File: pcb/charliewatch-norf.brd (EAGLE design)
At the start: 30.5 x 30.5 mm, 84 parts, among them U2 CC430F5137IRGZR, X1 CRYSTALS-NOGND-IQXC-25

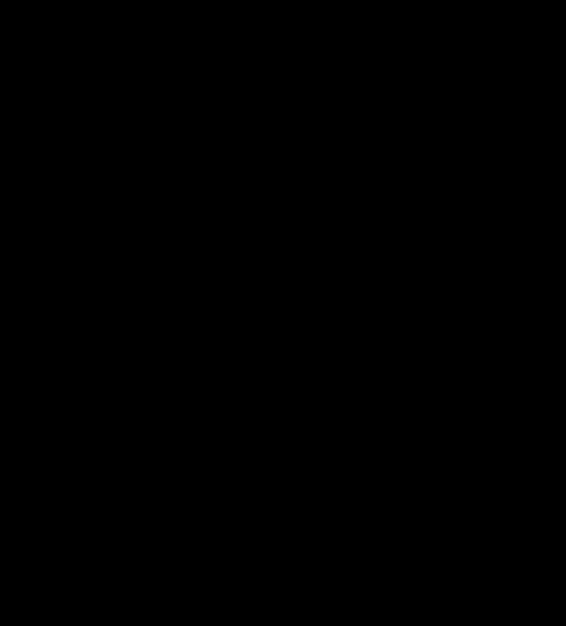
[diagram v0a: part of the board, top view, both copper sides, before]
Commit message: Add LIS3DH Accelerometer
LIS3DH is an i2c accelerometer. Hope to use this to control the watch
with tap based gestures
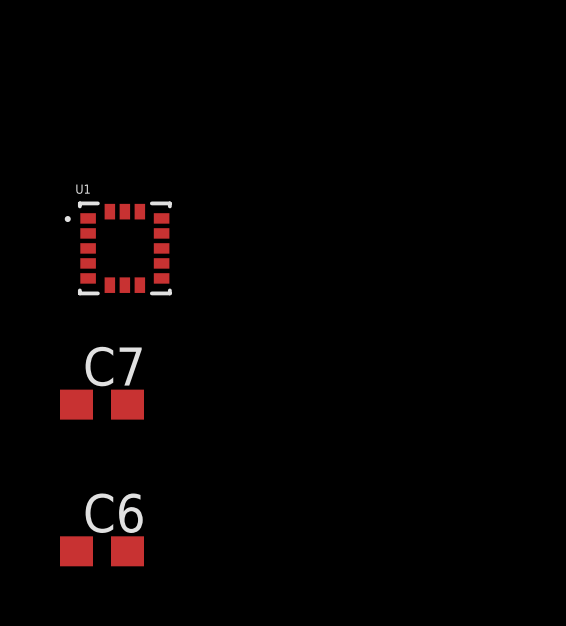
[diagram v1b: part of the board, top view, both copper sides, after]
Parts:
- added C6: 10uF, resistor:C0603
- added C7: 0.1uF, resistor:C0603
- added U1: LIS3DH, LIS3DH:PQFN50P300X300X100-16N
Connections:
- new net IMU_INT: U1.11, U2.13
- new net IMU_SCL: U1.4, U2.11
- new net IMU_SDA: U1.6, U2.10
- net GND: now also C6.2, C7.2, U1.10, U1.12, U1.5, U1.7
- net VCC: now also C6.1, C7.1, U1.1, U1.14, U1.8
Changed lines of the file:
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@@
 <?xml version="1.0" encoding="utf-8"?>
 <!DOCTYPE eagle SYSTEM "eagle.dtd">
-<eagle version="7.7.0">
+<eagle version="9.4.0">
 <drawing>
 <settings>
 <setting alwaysvectorfont="no"/>
+<setting keepoldvectorfont="yes"/>
 <setting verticaltext="up"/>
 </settings>
@@
 <param name="dpMaxLengthDifference" value="10mm"/>
 <param name="dpGapFactor" value="2.5"/>
-<param name="checkGrid" value="0"/>
 <param name="checkAngle" value="0"/>
 <param name="checkFont" value="1"/>
 <param name="checkRestrict" value="1"/>
+<param name="checkStop" value="0"/>
+<param name="checkValues" value="0"/>
+<param name="checkNames" value="1"/>
+<param name="checkWireStubs" value="1"/>
+<param name="checkPolygonWidth" value="0"/>
 <param name="useDiameter" value="13"/>
 <param name="maxErrors" value="50"/>
@@
 <element name="X1" library="IQD-Frequency-Products" package="2.0X1.2-2PAD" value="CRYSTALS-NOGND-IQXC-25" x="24.4475" y="31.115" smashed="yes" rot="R180"/>
 <element name="U2" library="Texas Instruments_By_element14_Batch_1" package="QFN50P700X700X100-49N" value="CC430F5137IRGZR" x="25.4" y="25.4" smashed="yes">
+<attribute name="MPN" value="CC430F5137IRGZR" x="25.4" y="25.4" size="1.778" layer="27" display="off"/>
+<attribute name="OC_FARNELL" value="-" x="25.4" y="25.4" size="1.778" layer="27" display="off"/>
+<attribute name="OC_NEWARK" value="68R5912" x="25.4" y="25.4" size="1.778" layer="27" display="off"/>
 <attribute name="PACKAGE" value="QFN-48" x="25.4" y="25.4" size="1.778" layer="27" display="off"/>
 <attribute name="SUPPLIER" value="TEXAS INSTRUMENTS" x="25.4" y="25.4" size="1.778" layer="27" display="off"/>
-<attribute name="OC_FARNELL" value="-" x="25.4" y="25.4" size="1.778" layer="27" display="off"/>
-<attribute name="MPN" value="CC430F5137IRGZR" x="25.4" y="25.4" size="1.778" layer="27" display="off"/>
-<attribute name="OC_NEWARK" value="68R5912" x="25.4" y="25.4" size="1.778" layer="27" display="off"/>
 </element>
 <element name="R1" library="rcl" package="R0402" value="75k" x="27.94" y="31.0515" smashed="yes">
@@
 </element>
 <element name="S2" library="SparkFun-Switches" package="TACTILE_SWITCH_SMD_RIGHT_ANGLE" value="MOMENTARY-SWITCH-SPST-SMD-RIGHT-ANGLE" x="38.1635" y="25.4" smashed="yes" rot="MR270">
+<attribute name="NAME" x="36.5125" y="25.4" size="0.6096" layer="26" font="vector" ratio="20" rot="MR270" align="bottom-center"/>
 <attribute name="PROD_ID" value="COMP-12265" x="38.1635" y="25.4" size="1.778" layer="28" rot="MR270" display="off"/>
-<attribute name="NAME" x="36.5125" y="25.4" size="0.6096" layer="26" font="vector" ratio="20" rot="MR270" align="bottom-center"/>
+</element>
+<element name="U1" library="LIS3DH" package="PQFN50P300X300X100-16N" value="LIS3DH" x="0.127" y="3.3655" smashed="yes">
+<attribute name="AVAILABILITY" value="Unavailable" x="-4.0005" y="8.509" size="1.778" layer="27" display="off"/>
+<attribute name="DESCRIPTION" value=" MEMS digital output motion sensor ultra low-power high performance 3-axes nano accelerometer " x="-4.0005" y="8.509" size="1.778" layer="27" display="off"/>
+<attribute name="MF" value="STMicroelectronics" x="-4.0005" y="8.509" size="1.778" layer="27" display="off"/>
+<attribute name="MP" value="LIS3DH" x="-4.0005" y="8.509" size="1.778" layer="27" display="off"/>
+<attribute name="NAME" x="-1.5242" y="5.18971875" size="0.3048375" layer="25"/>
+<attribute name="PACKAGE" value="LGA-16 STMicroelectronics" x="-4.0005" y="8.509" size="1.778" layer="27" display="off"/>
+<attribute name="PRICE" value="None" x="-4.0005" y="8.509" size="1.778" layer="27" display="off"/>
+<attribute name="VALUE" x="-1.6039" y="1.18336875" size="0.304959375" layer="27"/>
+</element>
+<element name="C6" library="resistor" package="C0603" value="10uF" x="-0.635" y="-6.731" smashed="yes">
+<attribute name="NAME" x="-1.27" y="-6.096" size="1.27" layer="25"/>
+<attribute name="VALUE" x="-1.27" y="-8.636" size="1.27" layer="27"/>
+</element>
+<element name="C7" library="resistor" package="C0603" value="0.1uF" x="-0.635" y="-1.8415" smashed="yes">
+<attribute name="NAME" x="-1.27" y="-1.2065" size="1.27" layer="25"/>
+<attribute name="VALUE" x="-1.27" y="-3.7465" size="1.27" layer="27"/>
 </element>
 </elements>
@@
 <wire x1="20.6375" y1="20.6375" x2="25.4" y2="25.4" width="0.8128" layer="16"/>
 <contactref element="S2" pad="1"/>
+<contactref element="U1" pad="5"/>
+<contactref element="U1" pad="10"/>
+<contactref element="U1" pad="12"/>
+<contactref element="C7" pad="2"/>
+<contactref element="C6" pad="2"/>
+<contactref element="U1" pad="7"/>
 <wire x1="26.9875" y1="24.4475" x2="38.1635" y2="27.35" width="0" layer="19" extent="16-16"/>
 <wire x1="25.654" y1="28.8798" x2="25.654" y2="27.3685" width="0" layer="19" extent="1-1"/>
+<wire x1="1.352" y1="3.8655" x2="19.05" y2="20.6375" width="0" layer="19" extent="1-1"/>
+<wire x1="1.352" y1="2.8655" x2="1.352" y2="3.8655" width="0" layer="19" extent="1-1"/>
+<wire x1="0.127" y1="2.1405" x2="1.352" y2="2.8655" width="0" layer="19" extent="1-1"/>
+<wire x1="-1.098" y1="2.3655" x2="0.127" y2="2.1405" width="0" layer="19" extent="1-1"/>
+<wire x1="0.215" y1="-1.8415" x2="0.127" y2="2.1405" width="0" layer="19" extent="1-1"/>
+<wire x1="0.215" y1="-6.731" x2="0.215" y2="-1.8415" width="0" layer="19" extent="1-1"/>
 </signal>
 <signal name="VCC">
@@
 <wire x1="29.464" y1="31.0515" x2="30.9245" y2="31.457" width="0.6096" layer="1"/>
 <wire x1="33.0835" y1="33.3375" x2="30.9245" y2="31.457" width="0.6096" layer="1"/>
+<contactref element="U1" pad="14"/>
+<contactref element="C7" pad="1"/>
+<contactref element="U1" pad="1"/>
+<contactref element="C6" pad="1"/>
+<contactref element="U1" pad="8"/>
 <wire x1="33.0835" y1="33.3375" x2="34.38025625" y2="34.380253125" width="0" layer="19" extent="16-16"/>
 <wire x1="26.162" y1="28.8798" x2="24.1554" y2="28.8798" width="0" layer="19" extent="1-1"/>
+<wire x1="0.627" y1="4.5905" x2="24.1554" y2="28.8798" width="0" layer="19" extent="1-1"/>
+<wire x1="-1.098" y1="4.3655" x2="0.627" y2="4.5905" width="0" layer="19" extent="1-1"/>
+<wire x1="0.627" y1="2.1405" x2="0.627" y2="4.5905" width="0" layer="19" extent="1-1"/>
+<wire x1="-1.485" y1="-1.8415" x2="0.627" y2="2.1405" width="0" layer="19" extent="1-1"/>
+<wire x1="-1.485" y1="-6.731" x2="-1.485" y2="-1.8415" width="0" layer="19" extent="1-1"/>
 </signal>
 <signal name="BSL_RST">
@@
 <contactref element="U2" pad="22"/>
 </signal>
+<signal name="IMU_INT">
+<contactref element="U1" pad="11"/>
+<contactref element="U2" pad="13"/>
+<wire x1="1.352" y1="3.3655" x2="22.6568" y2="21.9202" width="0" layer="19" extent="1-1"/>
+</signal>
+<signal name="IMU_SCL">
+<contactref element="U1" pad="4"/>
+<contactref element="U2" pad="11"/>
+<wire x1="-1.098" y1="2.8655" x2="21.9202" y2="23.1394" width="0" layer="19" extent="1-1"/>
+</signal>
+<signal name="IMU_SDA">
+<contactref element="U1" pad="6"/>
+<contactref element="U2" pad="10"/>
+<wire x1="-0.373" y1="2.1405" x2="21.9202" y2="23.6474" width="0" layer="19" extent="1-1"/>
+</signal>
 </signals>
+<mfgpreviewcolors>
+<mfgpreviewcolor name="soldermaskcolor" color="0xC8008000"/>
+<mfgpreviewcolor name="silkscreencolor" color="0xFFFEFEFE"/>
+<mfgpreviewcolor name="backgroundcolor" color="0xFF282828"/>
+<mfgpreviewcolor name="coppercolor" color="0xFFFFBF00"/>
+<mfgpreviewcolor name="substratecolor" color="0xFF786E46"/>
+</mfgpreviewcolors>
 <errors>
 </errors>

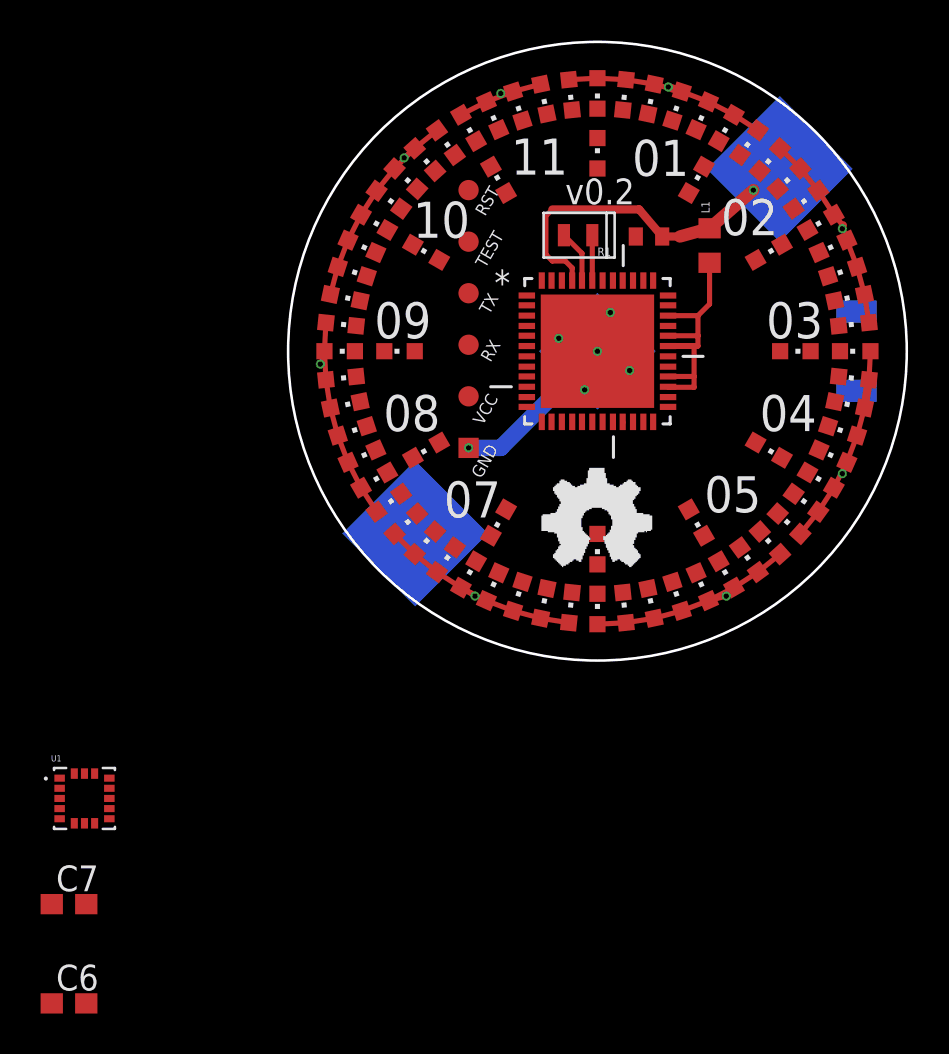
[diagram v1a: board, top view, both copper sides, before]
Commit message: Cleaned up .brd File
The Origin of the watch is (20, 20). Can now reference from that point
when designing
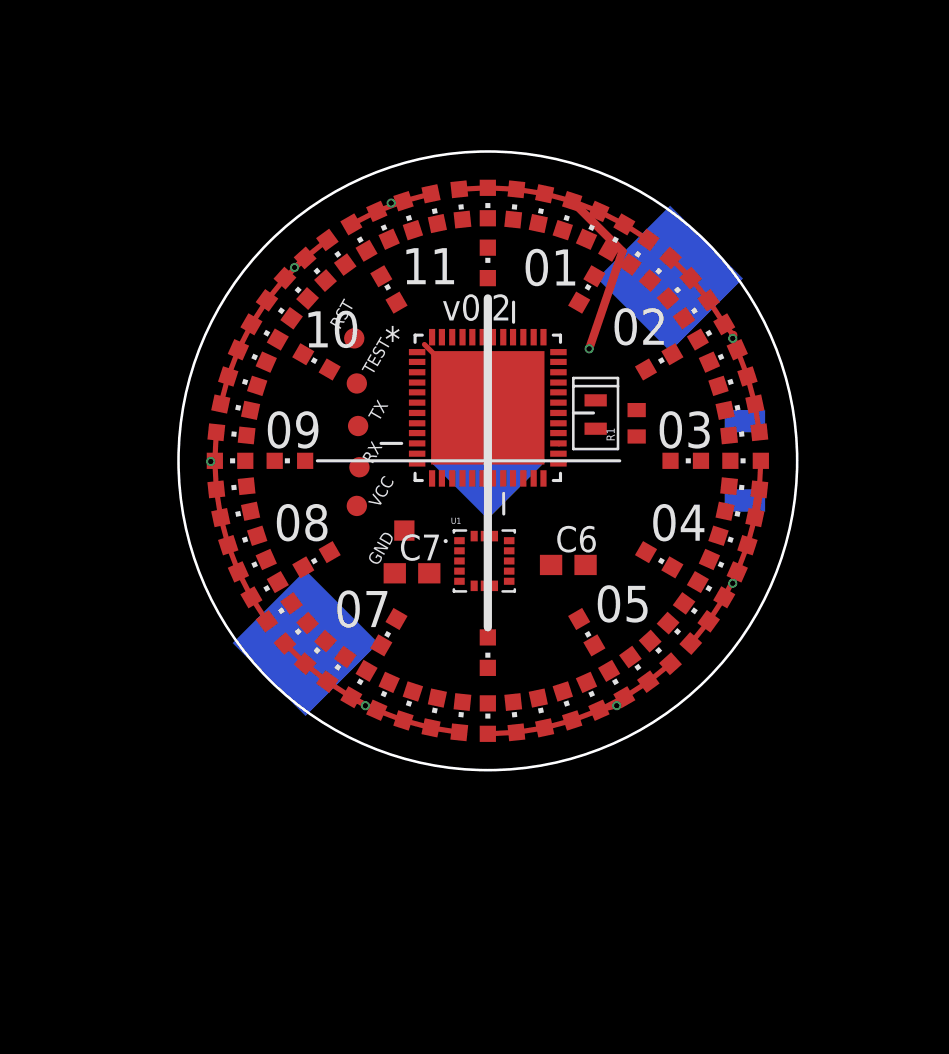
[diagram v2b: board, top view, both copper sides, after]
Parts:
- removed L1: (no value), rcl:R0603
- moved C6 32.7 mm to (24.0, 14.9)
- moved C7 23.5 mm to (16.3, 14.5)
- moved U1 22.9 mm to (19.8, 15.1)
- moved TP6 9.22 mm to (13.4, 26.0)
- moved R1 9.22 mm to (27.3, 21.8), turned to 90 degrees
- moved TP5 8.89 mm to (13.5, 23.8)
- moved X1 8.88 mm to (25.3, 22.3), turned to 270 degrees
- moved TP4 8.51 mm to (13.6, 21.7)
- moved TP3 8.08 mm to (13.7, 19.7)
- moved TP2 7.71 mm to (13.5, 17.8)
- moved S2 7.71 mm to (32.7, 20.0)
- moved LED13 7.64 mm to (30.3, 27.5)
- moved LED7 7.64 mm to (27.5, 30.3)
- moved LED21 7.64 mm to (31.0, 13.7)
- moved LED27 7.64 mm to (23.9, 7.92)
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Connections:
- net AVCC: no longer L1.1
- net VCC: no longer L1.2
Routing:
- net GND: track 21.2 -> 4.41 mm, vias 6 -> 0
- net VCC: track 15.9 -> 0.00 mm, vias 1 -> 0
- net AVCC: track 14.6 -> 0.04 mm
- net B0: track 10.6 -> 18.5 mm
- net XIN: track 2.60 -> 0.00 mm
- net XOUT: track 2.24 -> 0.00 mm
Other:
- board text removed: "https://trmm.net/Charliewatch"

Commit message: components place and laid out
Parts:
- moved X1 8.20 mm to (18.0, 26.0), turned to 180 degrees
- moved C6 7.02 mm to (17.0, 14.0), turned to 270 degrees
- moved R1 6.76 mm to (22.0, 26.0), turned to 0 degrees
- moved C7 6.75 mm to (23.0, 14.0), turned to 270 degrees
- moved U2 2.61 mm to (20.0, 20.0)
- moved TP1 2.10 mm to (13.9, 16.0), flipped to the bottom, turned to 90 degrees
- moved U1 1.08 mm to (20.0, 14.0), turned to 270 degrees
- moved TP6 0.53 mm to (13.6, 25.5), flipped to the bottom
- moved TP3 0.34 mm to (13.3, 19.7), flipped to the bottom
- moved TP4 0.22 mm to (13.4, 21.7), flipped to the bottom
- moved TP2 0.09 mm to (13.5, 17.8), flipped to the bottom
- moved TP5 0.09 mm to (13.5, 23.8), flipped to the bottom
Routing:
- net B0: track 18.5 -> 9.86 mm
- net GND: track 4.41 -> 0.00 mm

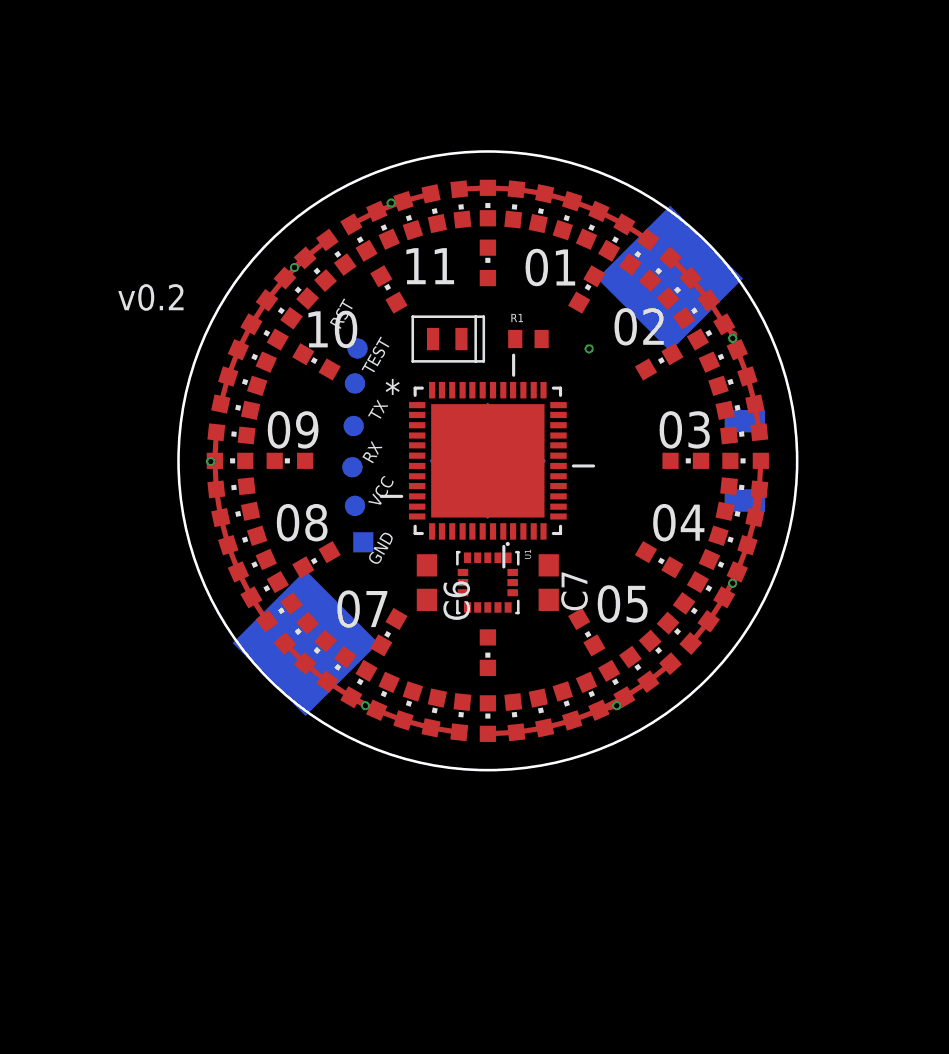
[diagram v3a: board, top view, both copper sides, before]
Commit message: Place programming pins
Also updated version to 0.3!
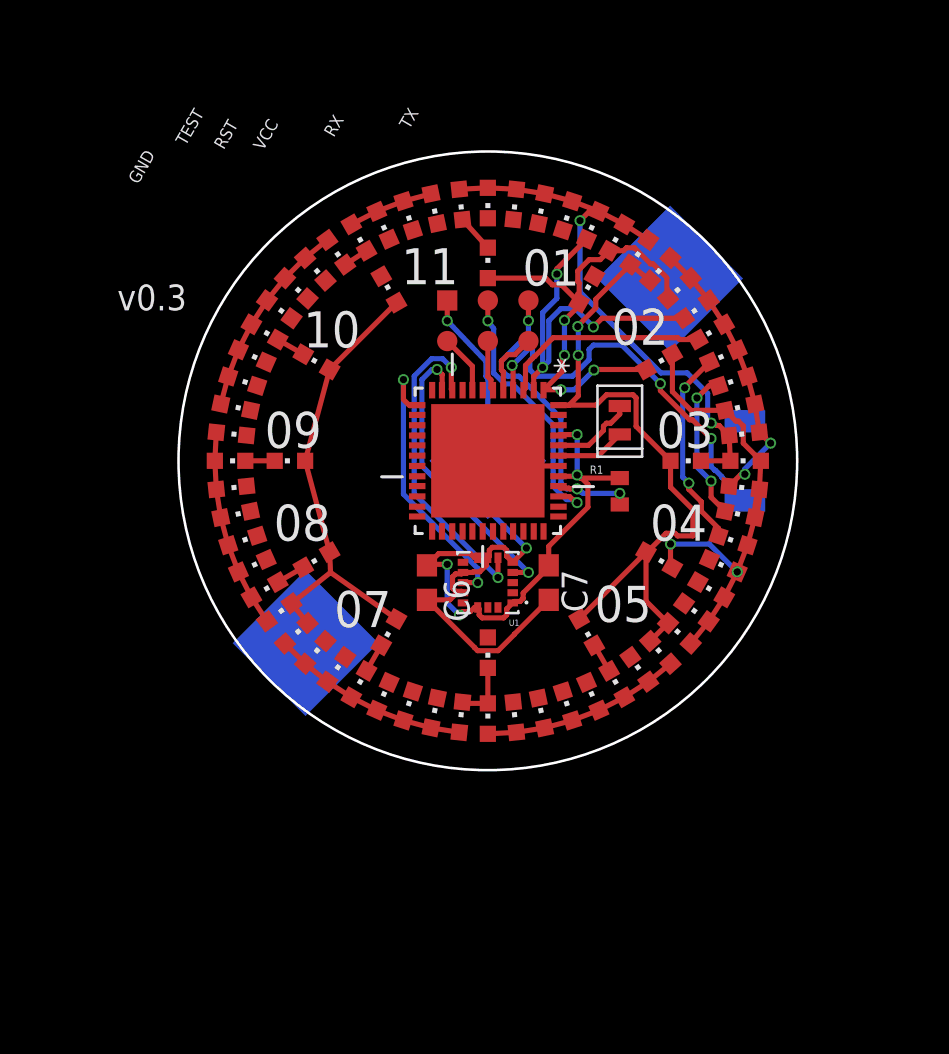
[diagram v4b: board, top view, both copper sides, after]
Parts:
- moved TP1 12.6 mm to (18.0, 27.9), flipped to the top, turned to 180 degrees
- moved TP4 9.57 mm to (22.0, 25.9), flipped to the top
- moved X1 9.39 mm to (26.5, 22.0), turned to 90 degrees
- moved TP2 9.31 mm to (18.0, 25.9), flipped to the top
- moved TP3 9.12 mm to (20.0, 25.9), flipped to the top
- moved R1 8.75 mm to (26.5, 18.5), turned to 90 degrees
- moved TP6 8.74 mm to (22.0, 27.9), flipped to the top
- moved TP5 7.72 mm to (20.0, 27.9), flipped to the top
- turned U1 to 180 degrees
- turned U2 to 270 degrees
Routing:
- net B8: track 0.00 -> 58.0 mm, vias 0 -> 2
- net GND: track 0.00 -> 33.9 mm, vias 0 -> 2
- net VCC: track 0.00 -> 24.5 mm, vias 0 -> 4
- net B7: track 4.84 -> 29.4 mm, vias 1 -> 4
- net B0: track 9.86 -> 31.2 mm, vias 1 -> 2
- net BUTTON: track 0.00 -> 19.8 mm, vias 0 -> 3
- net B6: track 10.6 -> 29.7 mm, vias 1 -> 3
- net IMU_SDA: track 0.00 -> 16.1 mm, vias 0 -> 2
- net BSL_RST: track 0.00 -> 15.7 mm, vias 0 -> 3
- net IMU_SCL: track 0.00 -> 14.5 mm, vias 0 -> 2
- net IMU_INT: track 0.00 -> 14.0 mm, vias 0 -> 2
- net BSL_TEST: track 0.00 -> 13.3 mm, vias 0 -> 2
- net B2: track 10.5 -> 23.1 mm, vias 1 -> 2
- net B5: track 10.1 -> 21.9 mm, vias 1 -> 0
- net B4: track 10.7 -> 19.7 mm, vias 1 -> 2
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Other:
- board text added: "v0.3"
- board text removed: "v0.2"

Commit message: Finish Routing
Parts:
- moved TP1 19.7 mm to (29.6, 12.0), flipped to the bottom
- moved TP5 17.6 mm to (27.6, 12.0), flipped to the bottom
- moved TP2 16.6 mm to (29.6, 14.0), flipped to the bottom
- moved TP6 16.3 mm to (25.6, 12.0), flipped to the bottom
- moved TP3 14.1 mm to (27.6, 14.0), flipped to the bottom
- moved C7 12.7 mm to (14.0, 23.0), turned to 180 degrees
- moved TP4 12.4 mm to (25.6, 14.0), flipped to the bottom
- moved R1 9.62 mm to (18.0, 14.0), turned to 0 degrees
- moved X1 9.18 mm to (22.0, 14.0), turned to 0 degrees
- moved U1 9.07 mm to (13.2, 20.0), turned to 90 degrees
- moved C6 4.24 mm to (14.0, 17.0), turned to 0 degrees
- turned U$1 to 135 degrees
- turned U2 to 180 degrees
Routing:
- net B4: track 19.7 -> 100.0 mm, vias 2 -> 10
- net B3: track 18.8 -> 94.7 mm, vias 2 -> 9
- net B2: track 23.1 -> 95.8 mm, vias 2 -> 13
- net B1: track 17.1 -> 88.0 mm, vias 2 -> 13
- net B5: track 21.9 -> 90.4 mm, vias 0 -> 8
- net B6: track 29.7 -> 97.5 mm, vias 3 -> 9
- net B7: track 29.4 -> 93.1 mm, vias 4 -> 13
- net B0: track 31.2 -> 83.2 mm, vias 2 -> 4
- net GND: track 33.9 -> 63.3 mm, vias 2 -> 6
- net B8: track 58.0 -> 78.3 mm, vias 2 -> 10
- net AVCC: track 0.00 -> 17.4 mm, vias 0 -> 3
- net VCC: track 24.5 -> 34.4 mm, vias 4 -> 8
- net BUTTON: track 19.8 -> 10.3 mm, vias 3 -> 1
- net BSL_VCC: track 2.93 -> 12.1 mm, vias 0 -> 1
- net BSL_RX: track 2.53 -> 9.23 mm, vias 0 -> 1
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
